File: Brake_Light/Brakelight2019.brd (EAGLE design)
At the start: 71.4 x 33.4 mm, 51 parts

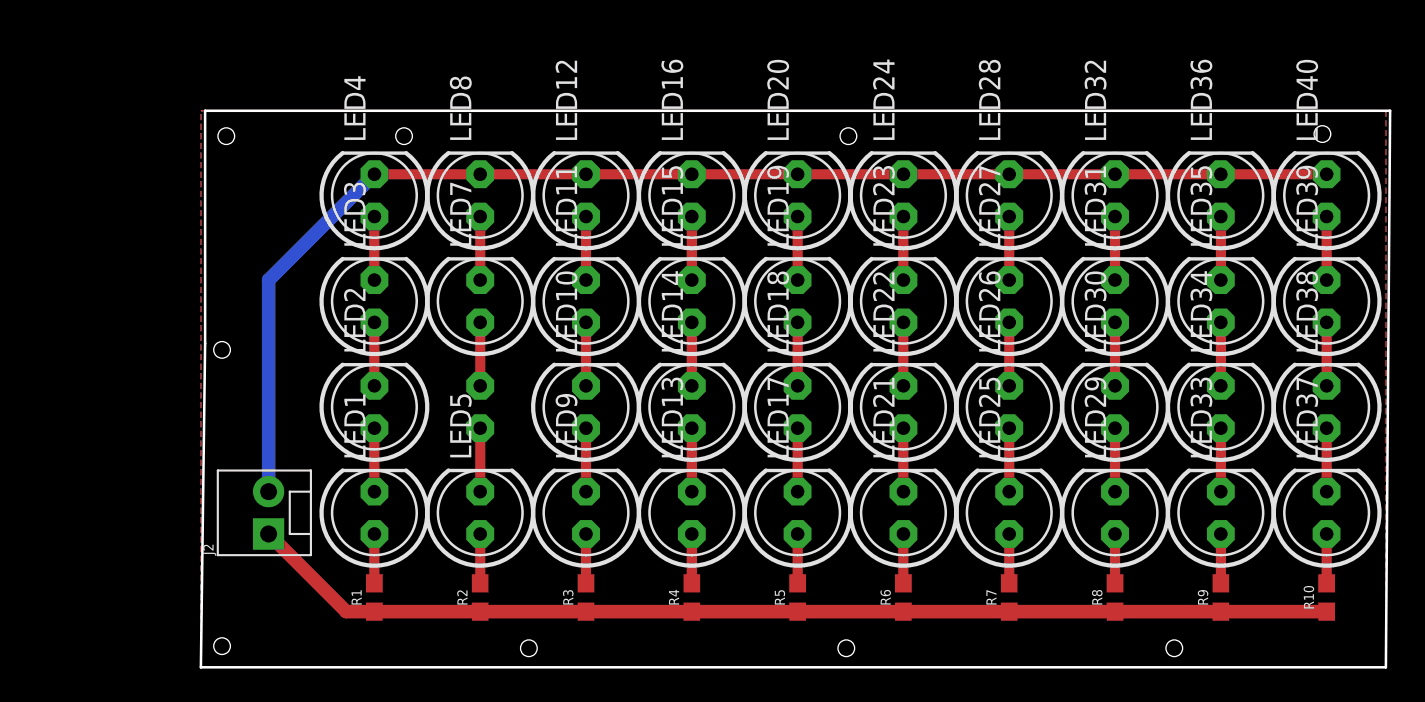
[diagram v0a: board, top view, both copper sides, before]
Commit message: Add files via upload
Changed the sizes & positions of the holes on the board
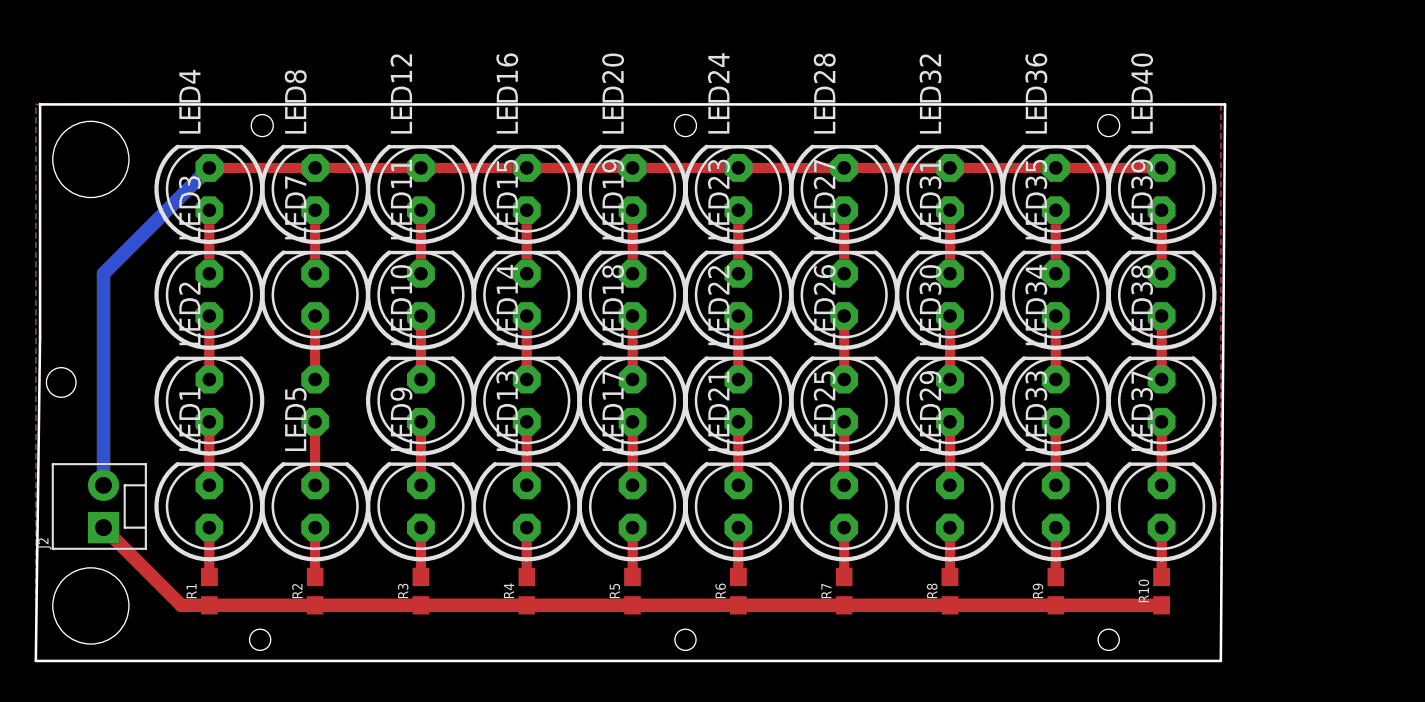
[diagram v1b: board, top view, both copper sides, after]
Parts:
- moved LED33 9.91 mm to (61.2, 9.27)
- moved LED34 9.91 mm to (61.2, 15.6)
- moved LED35 9.91 mm to (61.2, 22.0)
- moved LED36 9.91 mm to (61.2, 28.3)
- moved LED37 9.91 mm to (67.6, 9.27)
- moved LED38 9.91 mm to (67.6, 15.6)
- moved LED39 9.91 mm to (67.6, 22.0)
- moved LED40 9.91 mm to (67.6, 28.3)
- moved R10 9.91 mm to (67.6, 4.19)
- moved R9 9.91 mm to (61.2, 4.19)
- moved LED10 9.91 mm to (23.1, 15.6)
- moved LED11 9.91 mm to (23.1, 22.0)
- moved LED12 9.91 mm to (23.1, 28.3)
- moved LED5 9.91 mm to (16.8, 9.27)
- moved LED6 9.91 mm to (16.8, 15.6)
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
